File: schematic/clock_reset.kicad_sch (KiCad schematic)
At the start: 0 parts

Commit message: revised schematic into sheets for easier design. Looks much better.
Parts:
- added R60: 47R, symbol Device:R
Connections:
- new net ~{CLK}: R60.1
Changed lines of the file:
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@@
 (kicad_sch (version 20211123) (generator eeschema)
   (paper "A4")
+  (wire (pts (xy 74.295 71.12) (xy 78.74 71.12))
+    (stroke (width 0) (type default) (color 0 0 0 0))
+  )
+  (hierarchical_label "~{CLK}" (shape output) (at 74.295 71.12 180)
+    (effects (font (size 1.27 1.27)) (justify right))
+  )
+  (symbol (lib_id "Device:R") (at 82.55 71.12 90) (unit 1)
+    (in_bom yes) (on_board yes) (fields_autoplaced)
+    (property "Reference" "R60" (id 0) (at 82.55 65.405 90))
+    (property "Value" "47R" (id 1) (at 82.55 67.945 90))
+    (property "Footprint" "" (id 2) (at 82.55 72.898 90)
+      (effects (font (size 1.27 1.27)) hide)
+    )
+    (property "Datasheet" "~" (id 3) (at 82.55 71.12 0)
+      (effects (font (size 1.27 1.27)) hide)
+    )
+    (pin "1")
+    (pin "2")
+  )
 )

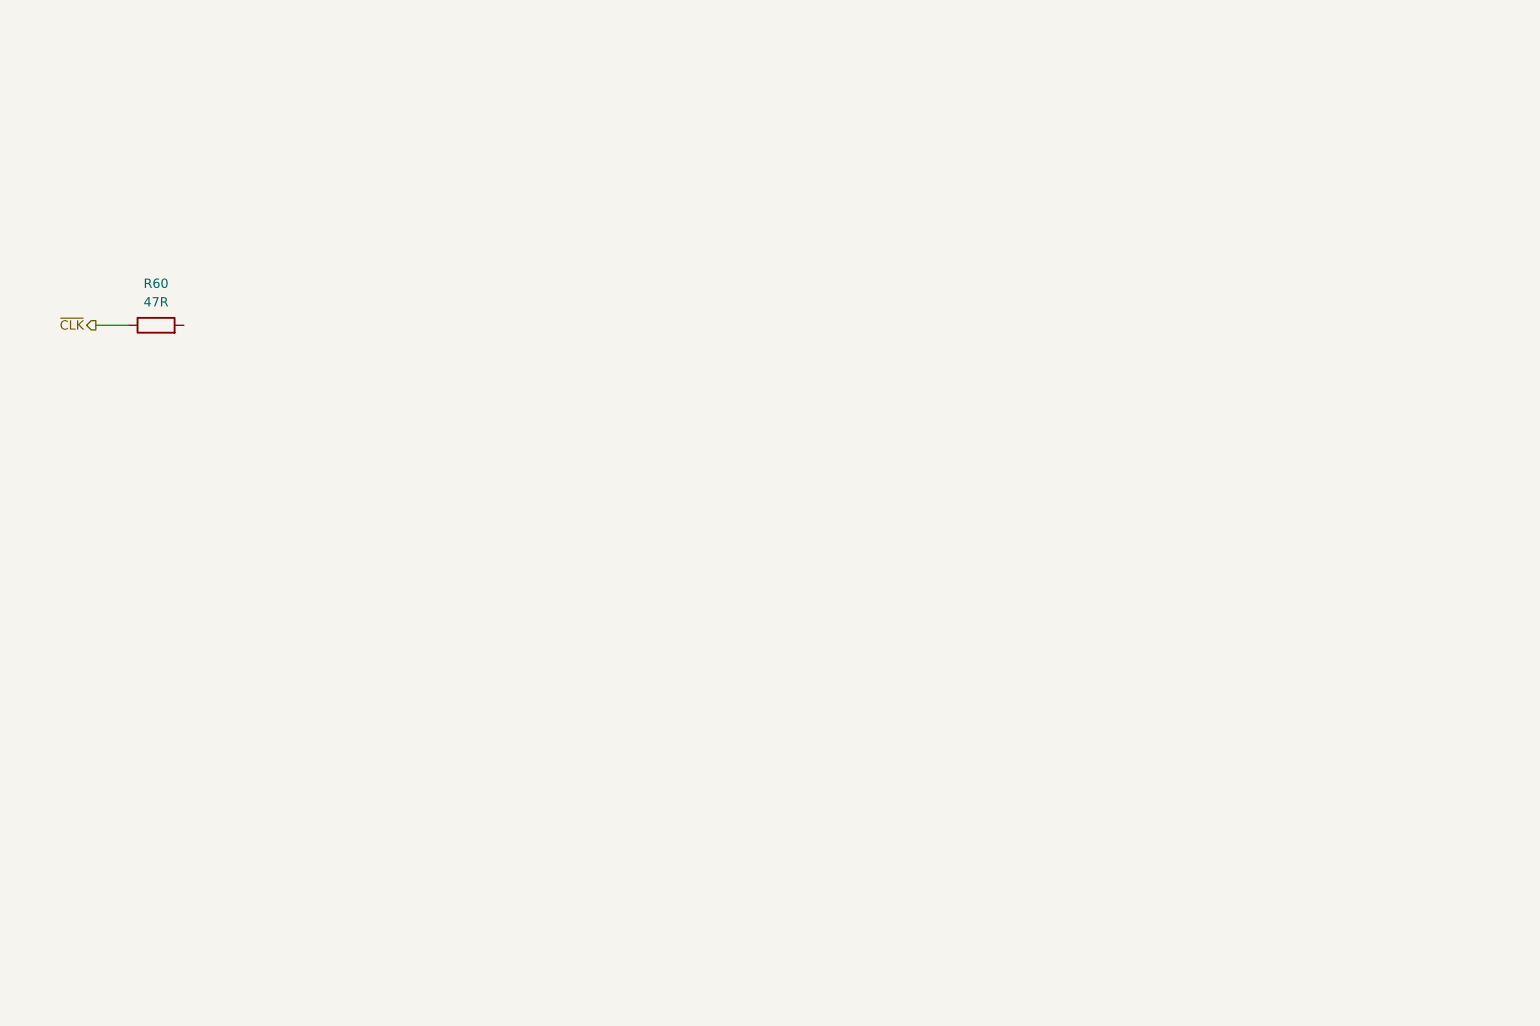
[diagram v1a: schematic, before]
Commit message: Up to pin 29 on z80 done. Address 0 to 10 left. Only tracing to its end point for the most part. Each chip gets traced chip to chip in this manned
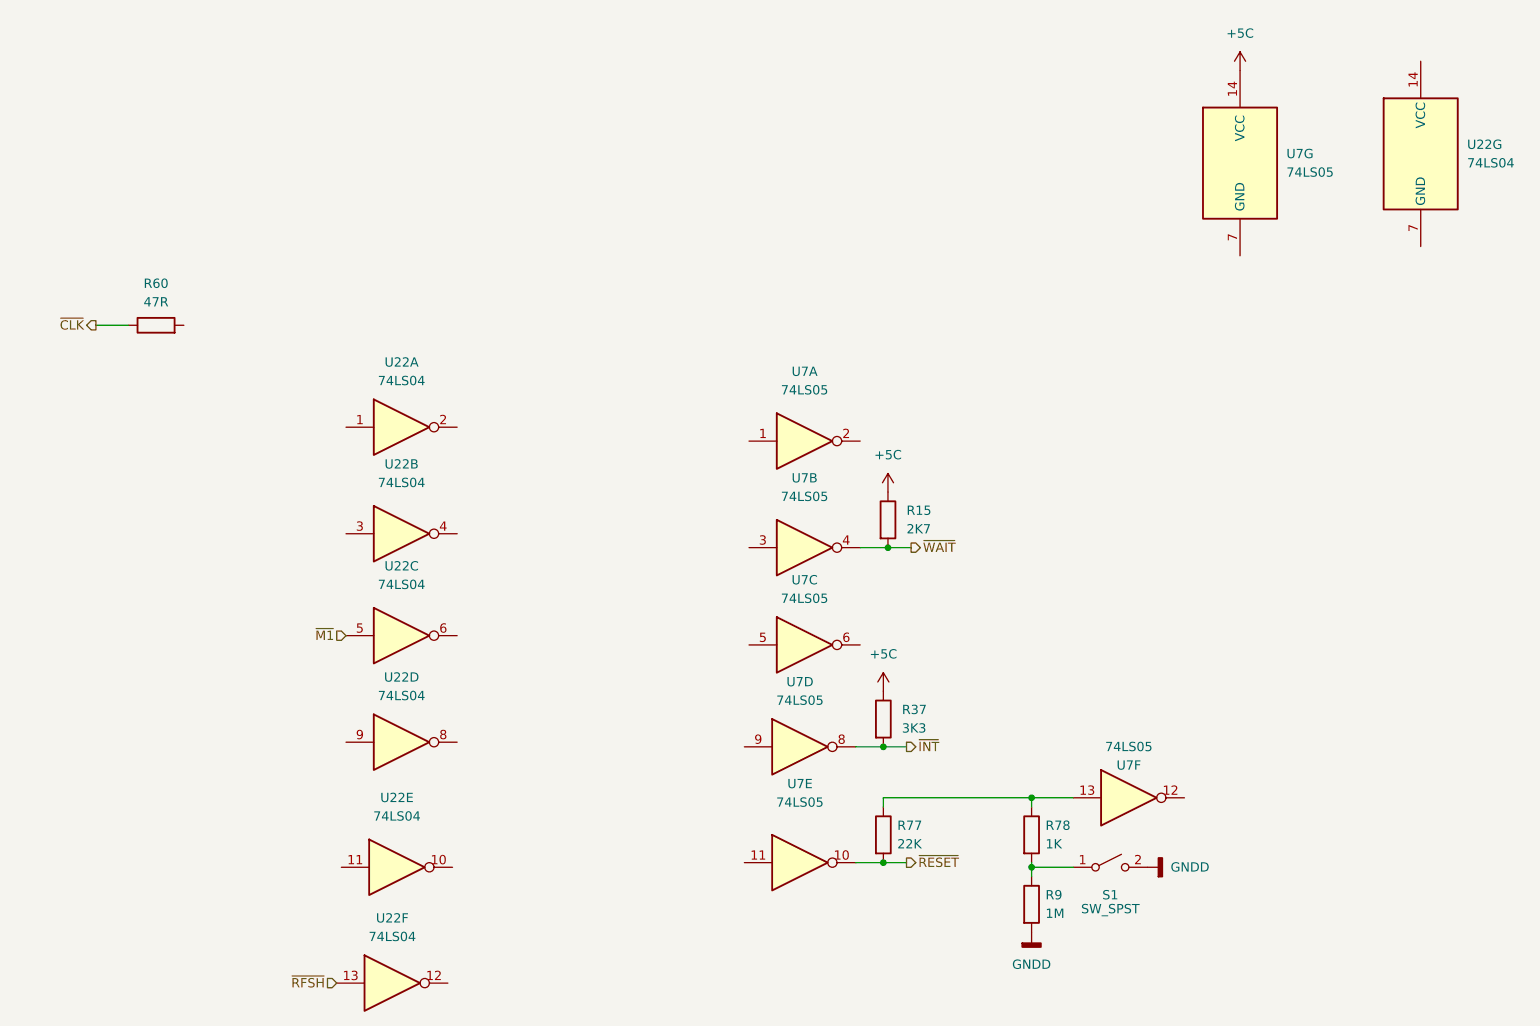
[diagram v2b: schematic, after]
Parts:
- added R15: 2K7, symbol Device:R
- added R37: 3K3, symbol Device:R
- added R77: 22K, symbol Device:R
- added R78: 1K, symbol Device:R
- added R9: 1M, symbol Device:R
- added S1: SW_SPST, symbol Switch:SW_SPST
- added U22: 74LS04, symbol 74xx:74LS04
- added U7: 74LS05, symbol 74xx:74LS05
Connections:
- new net: R78.2, R9.1, S1.1 (A)
- new net: R77.1, R78.1, U7.13
- new net +5C: R15.1, R37.1, U7.14 (VCC)
- new net GNDD: R9.2, S1.2 (B)
- new net ~{INT}: R37.2, U7.8
- new net ~{M1}: U22.5
- new net ~{RESET}: R77.2, U7.10
- new net ~{RFSH}: U22.13
- new net ~{WAIT}: R15.2, U7.4

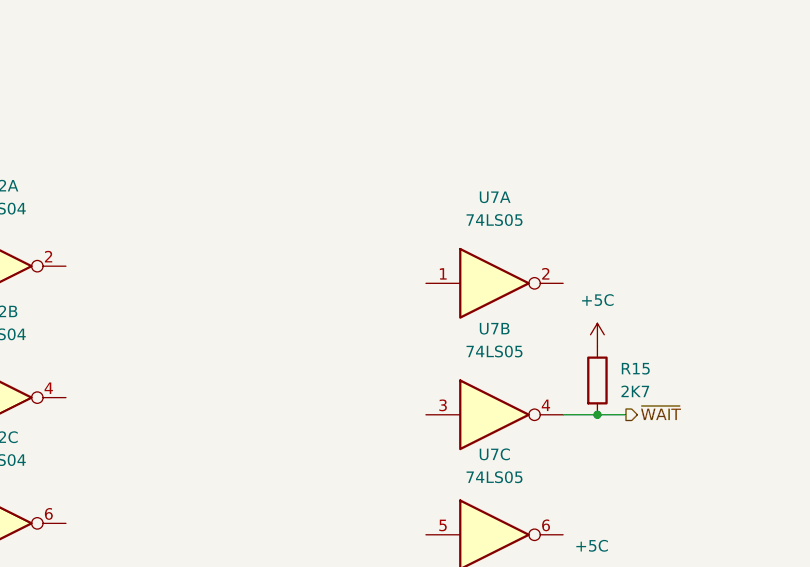
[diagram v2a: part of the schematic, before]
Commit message: completed Z80 trace of PCB. off to a good start.
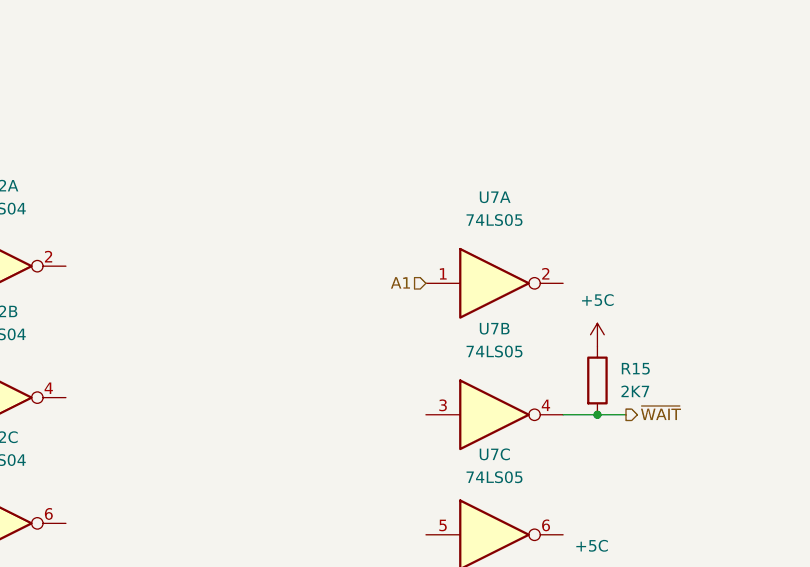
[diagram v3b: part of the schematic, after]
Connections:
- net A1: now reaches U7.1
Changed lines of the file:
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@@
+    (effects (font (size 1.27 1.27)) (justify right))
+  )
+  (hierarchical_label "A1" (shape input) (at 163.83 86.995 180)
     (effects (font (size 1.27 1.27)) (justify right))
   )

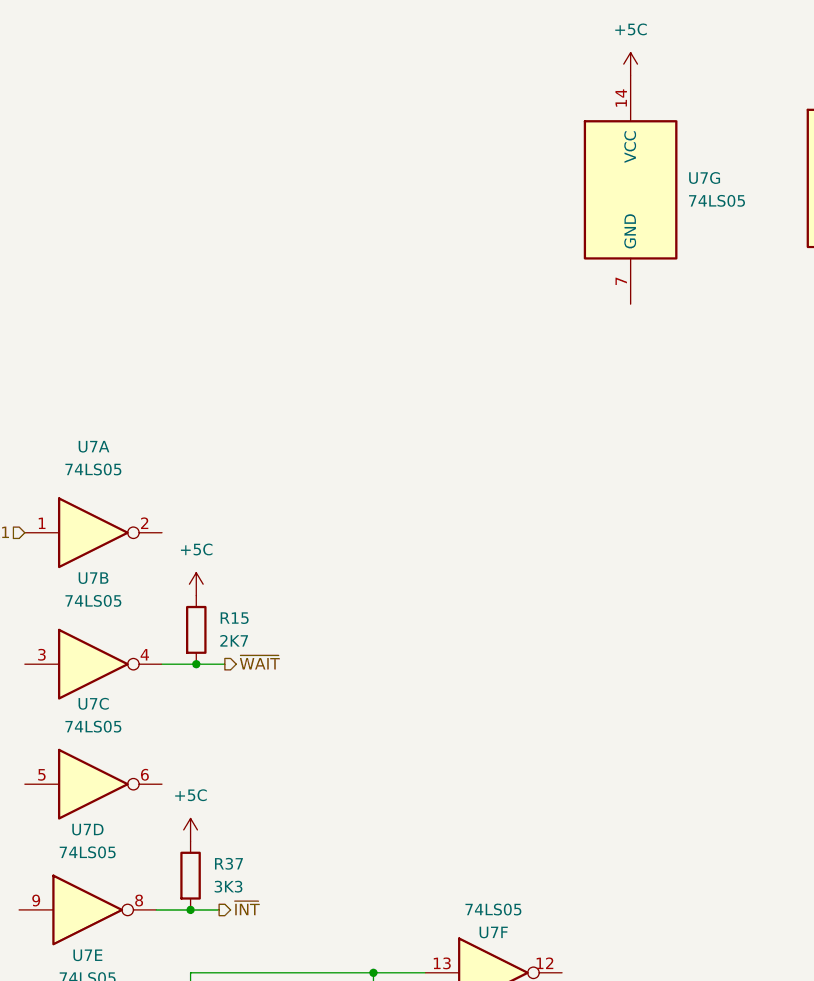
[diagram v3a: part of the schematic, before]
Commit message: added rf modulation schematic, added dram to vdp. Fixed +5vc to +5v
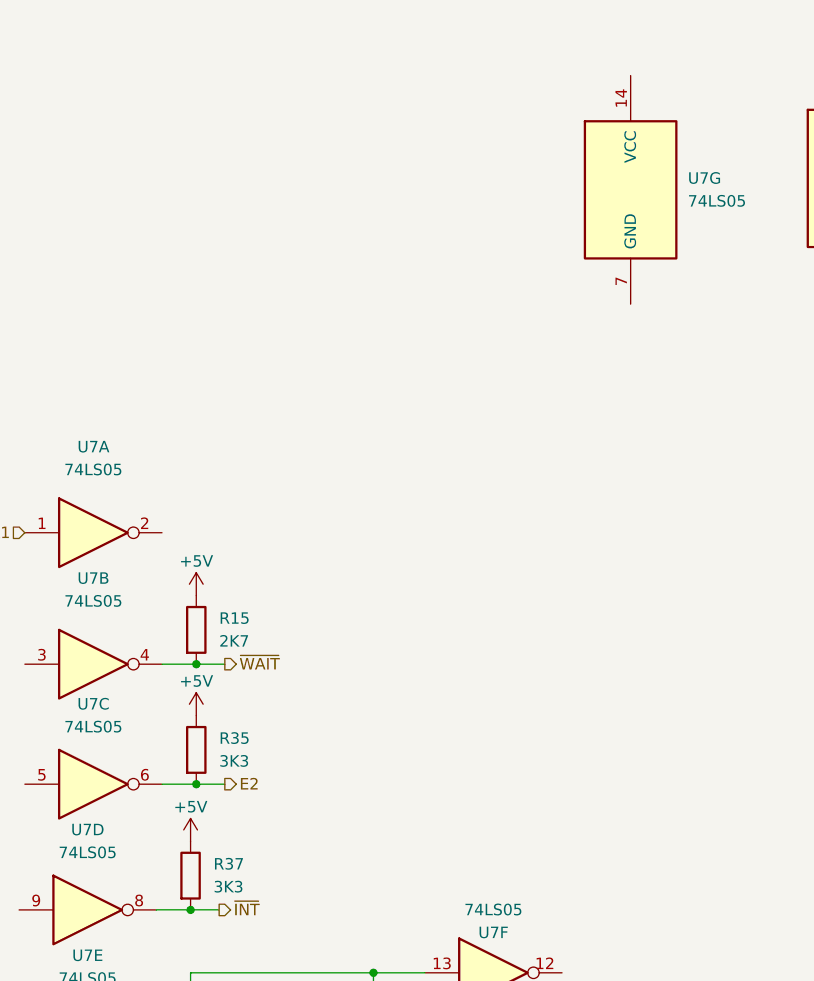
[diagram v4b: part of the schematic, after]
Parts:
- added R35: 3K3, symbol Device:R
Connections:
- net E2: now reaches U7.6
- net E2: now also R35.2
- net +5C renamed +5V
- net +5V: now also R35.1; no longer U7.14 (VCC)
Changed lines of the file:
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@@
   (junction (at 182.245 144.78) (diameter 0) (color 0 0 0 0)
   )
+  (junction (at 182.88 114.935) (diameter 0) (color 0 0 0 0)
+  )
   (wire (pts (xy 182.245 144.78) (xy 185.42 144.78))
     (stroke (width 0) (type default) (color 0 0 0 0))
@@
     (stroke (width 0) (type default) (color 0 0 0 0))
   )
+  (wire (pts (xy 179.07 114.935) (xy 182.88 114.935))
+    (stroke (width 0) (type default) (color 0 0 0 0))
+  )
   (wire (pts (xy 182.245 137.16) (xy 182.245 135.89))
     (stroke (width 0) (type default) (color 0 0 0 0))
   )
+  (wire (pts (xy 182.88 114.935) (xy 186.055 114.935))
+    (stroke (width 0) (type default) (color 0 0 0 0))
+  )
   (wire (pts (xy 179.07 101.6) (xy 182.88 101.6))
     (stroke (width 0) (type default) (color 0 0 0 0))
@@
   (wire (pts (xy 182.245 128.905) (xy 185.42 128.905))
     (stroke (width 0) (type default) (color 0 0 0 0))
+  )
+  (hierarchical_label "E2" (shape output) (at 186.055 114.935 0)
+    (effects (font (size 1.27 1.27)) (justify left))
   )
   (hierarchical_label "~{RFSH}" (shape input) (at 107.315 161.29 180)
@@
   (hierarchical_label "~{RESET}" (shape output) (at 185.42 144.78 0)
     (effects (font (size 1.27 1.27)) (justify left))
-  )
-  (symbol (lib_id "power:+5C") (at 182.245 121.285 0) (unit 1)
-    (in_bom yes) (on_board yes) (fields_autoplaced)
-    (property "Reference" "#PWR?" (id 0) (at 182.245 125.095 0)
-      (effects (font (size 1.27 1.27)) hide)
-    )
-    (property "Value" "+5C" (id 1) (at 182.245 116.205 0))
-    (property "Footprint" "" (id 2) (at 182.245 121.285 0)
-      (effects (font (size 1.27 1.27)) hide)
-    )
-    (property "Datasheet" "" (id 3) (at 182.245 121.285 0)
-      (effects (font (size 1.27 1.27)) hide)
-    )
-    (pin "1")
   )
   (symbol (lib_id "power:GNDD") (at 202.565 154.305 0) (unit 1)
@@
     (pin "7")
   )
+  (symbol (lib_id "power:+5V") (at 182.245 121.285 0) (unit 1)
+    (in_bom yes) (on_board yes)
+    (property "Reference" "#PWR?" (id 0) (at 182.245 125.095 0)
+      (effects (font (size 1.27 1.27)) hide)
+    )
+    (property "Value" "+5V" (id 1) (at 182.245 117.475 0))
+    (property "Footprint" "" (id 2) (at 182.245 121.285 0)
+      (effects (font (size 1.27 1.27)) hide)
+    )
+    (property "Datasheet" "" (id 3) (at 182.245 121.285 0)
+      (effects (font (size 1.27 1.27)) hide)
+    )
+    (pin "1")
+  )
   (symbol (lib_id "74xx:74LS05") (at 171.45 86.995 0) (unit 1)
     (in_bom yes) (on_board yes) (fields_autoplaced)
@@
     (pin "7")
   )
+  (symbol (lib_id "power:+5V") (at 182.88 93.98 0) (unit 1)
+    (in_bom yes) (on_board yes)
+    (property "Reference" "#PWR?" (id 0) (at 182.88 97.79 0)
+      (effects (font (size 1.27 1.27)) hide)
+    )
+    (property "Value" "+5V" (id 1) (at 182.88 90.17 0))
+    (property "Footprint" "" (id 2) (at 182.88 93.98 0)
+      (effects (font (size 1.27 1.27)) hide)
+    )
+    (property "Datasheet" "" (id 3) (at 182.88 93.98 0)
+      (effects (font (size 1.27 1.27)) hide)
+    )
+    (pin "1")
+  )
   (symbol (lib_id "74xx:74LS05") (at 171.45 101.6 0) (unit 2)
     (in_bom yes) (on_board yes) (fields_autoplaced)
@@
     (pin "7")
   )
-  (symbol (lib_id "power:+5C") (at 231.14 36.195 0) (unit 1)
-    (in_bom yes) (on_board yes) (fields_autoplaced)
-    (property "Reference" "#PWR?" (id 0) (at 231.14 40.005 0)
-      (effects (font (size 1.27 1.27)) hide)
-    )
-    (property "Value" "+5C" (id 1) (at 231.14 31.115 0))
-    (property "Footprint" "" (id 2) (at 231.14 36.195 0)
-      (effects (font (size 1.27 1.27)) hide)
-    )
-    (property "Datasheet" "" (id 3) (at 231.14 36.195 0)
-      (effects (font (size 1.27 1.27)) hide)
-    )
-    (pin "1")
-  )
   (symbol (lib_id "74xx:74LS04") (at 255.905 47.625 0) (unit 7)
     (in_bom yes) (on_board yes) (fields_autoplaced)
@@
     (pin "7")
   )
+  (symbol (lib_id "Device:R") (at 182.88 111.125 0) (unit 1)
+    (in_bom yes) (on_board yes) (fields_autoplaced)
+    (property "Reference" "R35" (id 0) (at 185.42 109.8549 0)
+      (effects (font (size 1.27 1.27)) (justify left))
+    )
+    (property "Value" "3K3" (id 1) (at 185.42 112.3949 0)
+      (effects (font (size 1.27 1.27)) (justify left))
+    )
+    (property "Footprint" "" (id 2) (at 181.102 111.125 90)
+      (effects (font (size 1.27 1.27)) hide)
+    )
+    (property "Datasheet" "~" (id 3) (at 182.88 111.125 0)
+      (effects (font (size 1.27 1.27)) hide)
+    )
+    (pin "1")
+    (pin "2")
+  )
   (symbol (lib_id "74xx:74LS05") (at 215.9 135.89 0) (unit 6)
     (in_bom yes) (on_board yes)
@@
     (pin "7")
   )
+  (symbol (lib_id "power:+5V") (at 182.88 107.315 0) (unit 1)
+    (in_bom yes) (on_board yes)
+    (property "Reference" "#PWR?" (id 0) (at 182.88 111.125 0)
+      (effects (font (size 1.27 1.27)) hide)
+    )
+    (property "Value" "+5V" (id 1) (at 182.88 103.505 0))
+    (property "Footprint" "" (id 2) (at 182.88 107.315 0)
+      (effects (font (size 1.27 1.27)) hide)
+    )
+    (property "Datasheet" "" (id 3) (at 182.88 107.315 0)
+      (effects (font (size 1.27 1.27)) hide)
+    )
+    (pin "1")
+  )
   (symbol (lib_id "Device:R") (at 202.565 140.97 0) (unit 1)
     (in_bom yes) (on_board yes) (fields_autoplaced)
@@
     (pin "2")
   )
-  (symbol (lib_id "power:+5C") (at 182.88 93.98 0) (unit 1)
-    (in_bom yes) (on_board yes) (fields_autoplaced)
-    (property "Reference" "#PWR?" (id 0) (at 182.88 97.79 0)
-      (effects (font (size 1.27 1.27)) hide)
-    )
-    (property "Value" "+5C" (id 1) (at 182.88 88.9 0))
-    (property "Footprint" "" (id 2) (at 182.88 93.98 0)
-      (effects (font (size 1.27 1.27)) hide)
-    )
-    (property "Datasheet" "" (id 3) (at 182.88 93.98 0)
-      (effects (font (size 1.27 1.27)) hide)
-    )
-    (pin "1")
-  )
   (symbol (lib_id "74xx:74LS04") (at 116.205 99.695 0) (unit 2)
